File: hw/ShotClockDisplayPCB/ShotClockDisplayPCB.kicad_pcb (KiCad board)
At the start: 4 copper layers, 54.5 x 54 mm, 5 parts, among them J1 Conn_01x05_Socket, J2 Conn_01x05_Socket, J3 Conn_01x05_Socket, J4 Conn_01x05_Socket, J5 Conn_01x06_Pin

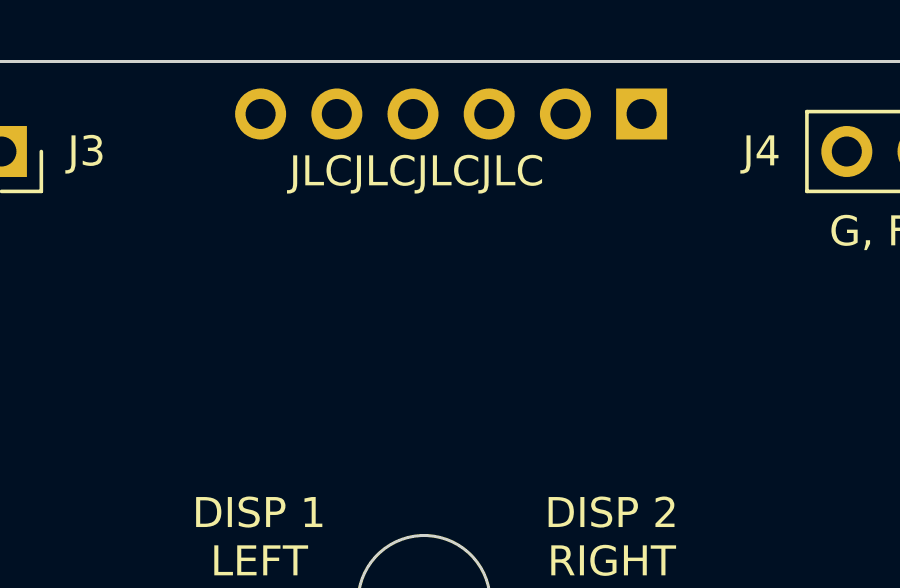
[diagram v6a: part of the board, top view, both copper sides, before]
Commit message: Changed display connectors to JST PH 2.0mm
In docs, schematic and footprints
Both sides, connect with male/male cable
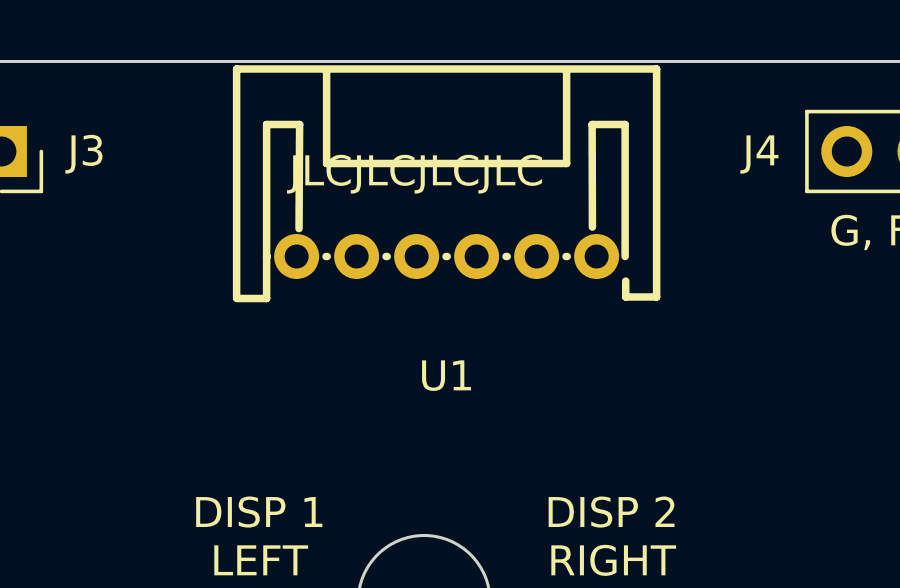
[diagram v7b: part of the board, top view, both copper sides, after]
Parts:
- removed J5: Conn_01x06_Pin, Connector_PinHeader_2.54mm:PinHeader_1x06_P2.54mm_Vertical
- added U1: S6B-PH-K-S-(LF)(SN), S6B_PH_K_S_LF_SN:CONN-TH_6P-P2.00_S6B-PH-K-S-LF-SN, F.Cu at (53.2, 31.5)
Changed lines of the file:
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@@
+    )
+  )
+  (footprint "S6B_PH_K_S_LF_SN:CONN-TH_6P-P2.00_S6B-PH-K-S-LF-SN" (layer "F.Cu")
+    (at 53.25 31.5 180)
+    (property "LCSC Part" "C157920")
+    (property "Sheetfile" "mainboard_connectors.kicad_sch")
+    (property "Sheetname" "MainBoardConnectors")
+    (attr smd)
+    (fp_text reference "U1" (at 0 -4) (layer "F.SilkS")
+        (effects (font (size 1 1) (thickness 0.15)))
+    )
+    (fp_text value "S6B-PH-K-S-(LF)(SN)" (at 0 4) (layer "F.Fab")
+        (effects (font (size 1 1) (thickness 0.15)))
+    )
+    (fp_text user "${REFERENCE}" (at 0 0) (layer "F.Fab")
+        (effects (font (size 1 1) (thickness 0.15)))
+    )
+    (fp_line (start -7 -1.35) (end -5.97 -1.35)
+      (stroke (width 0.25) (type solid)) (layer "F.SilkS"))
+    (fp_line (start -7 6.25) (end -7 -1.35)
+      (stroke (width 0.25) (type solid)) (layer "F.SilkS"))
+    (fp_line (start -5.97 -1.35) (end -5.97 -0.82)
+      (stroke (width 0.25) (type solid)) (layer "F.SilkS"))
+    (fp_line (start -5.95 4.4) (end -5.95 0)
+      (stroke (width 0.25) (type solid)) (layer "F.SilkS"))
+    (fp_line (start -4.86 0.98) (end -4.85 4.4)
+      (stroke (width 0.25) (type solid)) (layer "F.SilkS"))
+    (fp_line (start -4.85 4.4) (end -5.95 4.4)
+      (stroke (width 0.25) (type solid)) (layer "F.SilkS"))
+    (fp_line (start -4.02 0) (end -3.98 0)
+      (stroke (width 0.25) (type solid)) (layer "F.SilkS"))
+    (fp_line (start -4 3.1) (end -4 6.2)
+      (stroke (width 0.25) (type solid)) (layer "F.SilkS"))
+    (fp_line (start -2.02 0) (end -1.98 0)
+      (stroke (width 0.25) (type solid)) (layer "F.SilkS"))
+    (fp_line (start -0.02 0) (end 0.02 0)
+      (stroke (width 0.25) (type solid)) (layer "F.SilkS"))
+    (fp_line (start 1.98 0) (end 2.02 0)
+      (stroke (width 0.25) (type solid)) (layer "F.SilkS"))
+    (fp_line (start 3.98 0) (end 4.02 0)
+      (stroke (width 0.25) (type solid)) (layer "F.SilkS"))
+    (fp_line (start 4 3.1) (end -4 3.1)
+      (stroke (width 0.25) (type solid)) (layer "F.SilkS"))
+    (fp_line (start 4 6.2) (end 4 3.1)
+      (stroke (width 0.25) (type solid)) (layer "F.SilkS"))
+    (fp_line (start 4.9 4.4) (end 4.92 0.93)
+      (stroke (width 0.25) (type solid)) (layer "F.SilkS"))
+    (fp_line (start 5.98 0) (end 6 0)
+      (stroke (width 0.25) (type solid)) (layer "F.SilkS"))
+    (fp_line (start 6 -1.4) (end 7 -1.4)
+      (stroke (width 0.25) (type solid)) (layer "F.SilkS"))
+    (fp_line (start 6 0) (end 6 -1.4)
+      (stroke (width 0.25) (type solid)) (layer "F.SilkS"))
+    (fp_line (start 6 0) (end 6 4.4)
+      (stroke (width 0.25) (type solid)) (layer "F.SilkS"))
+    (fp_line (start 6 4.4) (end 4.9 4.4)
+      (stroke (width 0.25) (type solid)) (layer "F.SilkS"))
+    (fp_line (start 7 -1.35) (end 7 6.25)
+      (stroke (width 0.25) (type solid)) (layer "F.SilkS"))
+    (fp_line (start 7 6.25) (end -7 6.25)
+      (stroke (width 0.25) (type solid)) (layer "F.SilkS"))
+    (fp_circle (center -6.95 6.25) (end -6.92 6.25)
+      (stroke (width 0.06) (type solid)) (fill none) (layer "F.Fab"))
+    (pad "1" thru_hole circle (at -5 0) (size 1.5 1.5) (drill 0.799998) (layers "*.Cu" "*.Paste" "*.Mask")
+      (net 19 "/MainBoardConnectors/TLC59116_RESETn") (pinfunction "1") (pintype "passive"))
+    (pad "2" thru_hole circle (at -3 0) (size 1.5 1.5) (drill 0.799998) (layers "*.Cu" "*.Paste" "*.Mask")
+      (net 20 "+3.3V") (pinfunction "2") (pintype "passive"))
+    (pad "3" thru_hole circle (at -1 0) (size 1.5 1.5) (drill 0.799998) (layers "*.Cu" "*.Paste" "*.Mask")
+      (net 1 "+5V") (pinfunction "3") (pintype "passive"))
+    (pad "4" thru_hole circle (at 1 0) (size 1.5 1.5) (drill 0.799998) (layers "*.Cu" "*.Paste" "*.Mask")
+      (net 21 "/MainBoardConnectors/I2C1_SCL") (pinfunction "4") (pintype "passive"))
+    (pad "5" thru_hole circle (at 3 0) (size 1.5 1.5) (drill 0.799998) (layers "*.Cu" "*.Paste" "*.Mask")
+      (net 22 "/MainBoardConnectors/I2C1_SDA") (pinfunction "5") (pintype "passive"))
+    (pad "6" thru_hole circle (at 5 0) (size 1.5 1.5) (drill 0.799998) (layers "*.Cu" "*.Paste" "*.Mask")
+      (net 2 "GND") (pinfunction "6") (pintype "passive"))
+    (model "/home/mats/GitHub/KiCad7SymbolsAndFootprints/PartLibraries/EasyEDA/S6B_PH_K_S_LF_SN/S6B_PH_K_S_LF_SN.3dshapes/CONN-TH_6P-P2.00_S6B-PH-K-S-LF-SN.wrl"
+      (offset (xyz 0 -2.35 0.25))
+      (scale (xyz 1 1 1))
+      (rotate (xyz 0 0 0))
     )
   )
@@
       (offset (xyz 0 0 0))
       (scale (xyz 1 1 1))
-      (rotate (xyz 0 0 0))
-    )
-  )
-  (footprint "Connector_PinHeader_2.54mm:PinHeader_1x06_P2.54mm_Vertical" (layer "B.Cu")
-    (at 59.75 26.75 90)
-    (descr "Through hole straight pin header, 1x06, 2.54mm pitch, single row")
-    (tags "Through hole pin header THT 1x06 2.54mm single row")
-    (property "LCSC Part" "C37208")
-    (property "LCSC Part #" "C37208")
-    (property "Sheetfile" "mainboard_connectors.kicad_sch")
-    (property "Sheetname" "MainBoardConnectors")
-    (property "ki_description" "Generic connector, single row, 01x06, script generated")
-    (property "ki_keywords" "connector")
-    (attr through_hole)
-    (fp_text reference "J5" (at 0 2.33 90) (layer "B.SilkS")
-        (effects (font (size 1 1) (thickness 0.15)) (justify mirror))
-    )
-    (fp_text value "Conn_01x06_Pin" (at 0 -15.03 90) (layer "B.Fab")
-        (effects (font (size 1 1) (thickness 0.15)) (justify mirror))
-    )
-    (fp_text user "${REFERENCE}" (at 0 -6.35) (layer "B.Fab")
-        (effects (font (size 1 1) (thickness 0.15)) (justify mirror))
-    )
-    (fp_line (start -1.33 -14.03) (end 1.33 -14.03)
-      (stroke (width 0.12) (type solid)) (layer "B.SilkS"))
-    (fp_line (start -1.33 -1.27) (end -1.33 -14.03)
-      (stroke (width 0.12) (type solid)) (layer "B.SilkS"))
-    (fp_line (start -1.33 -1.27) (end 1.33 -1.27)
-      (stroke (width 0.12) (type solid)) (layer "B.SilkS"))
-    (fp_line (start -1.33 0) (end -1.33 1.33)
-      (stroke (width 0.12) (type solid)) (layer "B.SilkS"))
-    (fp_line (start -1.33 1.33) (end 0 1.33)
-      (stroke (width 0.12) (type solid)) (layer "B.SilkS"))
-    (fp_line (start 1.33 -1.27) (end 1.33 -14.03)
-      (stroke (width 0.12) (type solid)) (layer "B.SilkS"))
-    (fp_line (start -1.8 -14.5) (end 1.8 -14.5)
-      (stroke (width 0.05) (type solid)) (layer "B.CrtYd"))
-    (fp_line (start -1.8 1.8) (end -1.8 -14.5)
-      (stroke (width 0.05) (type solid)) (layer "B.CrtYd"))
-    (fp_line (start 1.8 -14.5) (end 1.8 1.8)
-      (stroke (width 0.05) (type solid)) (layer "B.CrtYd"))
-    (fp_line (start 1.8 1.8) (end -1.8 1.8)
-      (stroke (width 0.05) (type solid)) (layer "B.CrtYd"))
-    (fp_line (start -1.27 -13.97) (end -1.27 0.635)
-      (stroke (width 0.1) (type solid)) (layer "B.Fab"))
-    (fp_line (start -1.27 0.635) (end -0.635 1.27)
-      (stroke (width 0.1) (type solid)) (layer "B.Fab"))
-    (fp_line (start -0.635 1.27) (end 1.27 1.27)
-      (stroke (width 0.1) (type solid)) (layer "B.Fab"))
-    (fp_line (start 1.27 -13.97) (end -1.27 -13.97)
-      (stroke (width 0.1) (type solid)) (layer "B.Fab"))
-    (fp_line (start 1.27 1.27) (end 1.27 -13.97)
-      (stroke (width 0.1) (type solid)) (layer "B.Fab"))
-    (pad "1" thru_hole rect (at 0 0 90) (size 1.7 1.7) (drill 1) (layers "*.Cu" "*.Mask")
-      (net 19 "/MainBoardConnectors/TLC59116_RESETn") (pinfunction "Pin_1") (pintype "passive"))
-    (pad "2" thru_hole oval (at 0 -2.54 90) (size 1.7 1.7) (drill 1) (layers "*.Cu" "*.Mask")
-      (net 20 "+3.3V") (pinfunction "Pin_2") (pintype "passive"))
-    (pad "3" thru_hole oval (at 0 -5.08 90) (size 1.7 1.7) (drill 1) (layers "*.Cu" "*.Mask")
-      (net 1 "+5V") (pinfunction "Pin_3") (pintype "passive"))
-    (pad "4" thru_hole oval (at 0 -7.62 90) (size 1.7 1.7) (drill 1) (layers "*.Cu" "*.Mask")
-      (net 21 "/MainBoardConnectors/I2C1_SCL") (pinfunction "Pin_4") (pintype "passive"))
-    (pad "5" thru_hole oval (at 0 -10.16 90) (size 1.7 1.7) (drill 1) (layers "*.Cu" "*.Mask")
-      (net 22 "/MainBoardConnectors/I2C1_SDA") (pinfunction "Pin_5") (pintype "passive"))
-    (pad "6" thru_hole oval (at 0 -12.7 90) (size 1.7 1.7) (drill 1) (layers "*.Cu" "*.Mask")
-      (net 2 "GND") (pinfunction "Pin_6") (pintype "passive"))
-    (model "${KICAD6_3DMODEL_DIR}/Connector_PinHeader_2.54mm.3dshapes/PinHeader_1x06_P2.54mm_Vertical.wrl"
-      (offset (xyz 0 0 0))
-      (scale (xyz 1 1 1))
